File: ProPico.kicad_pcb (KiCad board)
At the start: 2 copper layers, 21 x 51 mm, 56 parts, among them J1 USB_C_Receptacle_USB2.0, J2 SWD, J3 LEFT, J4 RIGHT, SW1 BOOTSEL, SW2 RES, U1 FM24CL16B, U2 W25Q16JVUXIQ, U3 AMS1117-3.3, U4 LM4040DBZ-3, U5 RP2040, Y1 ECS-120-12-36-AGN-TR3

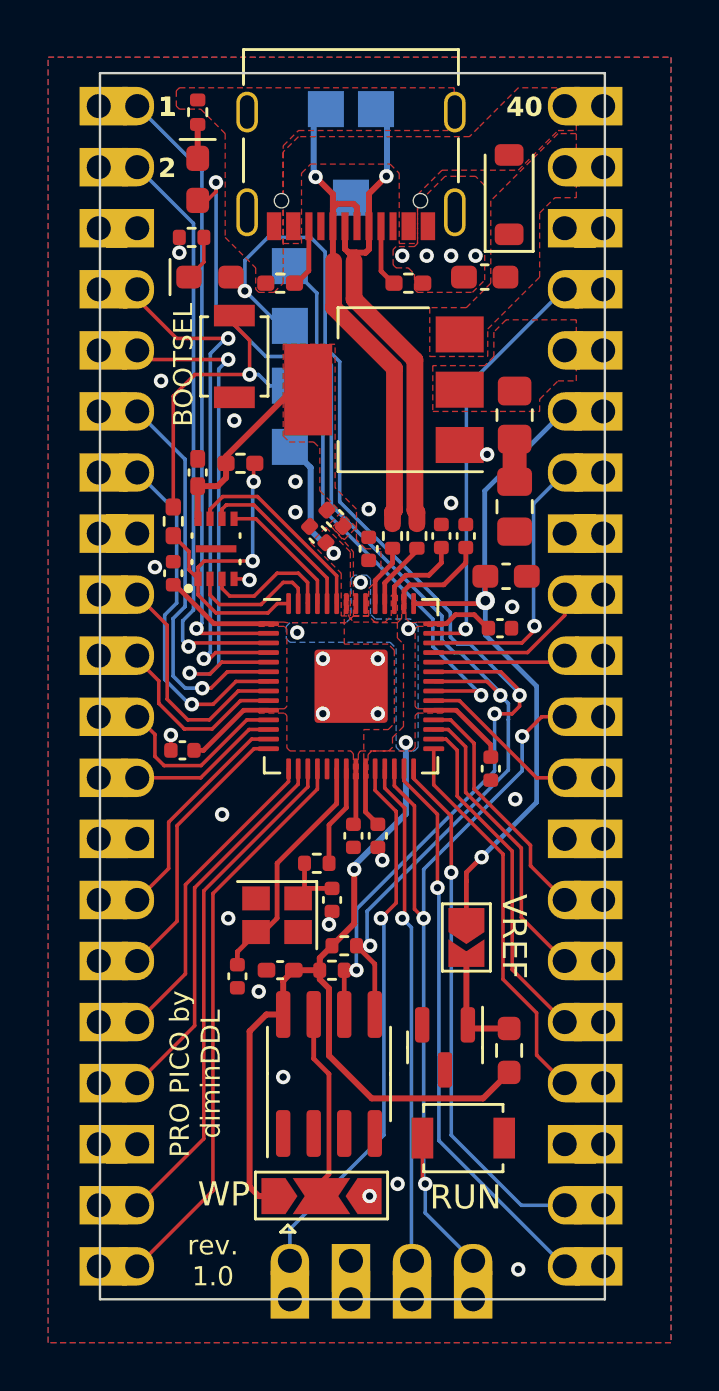
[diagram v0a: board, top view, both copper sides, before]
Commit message: Changed LDO for lower dropout
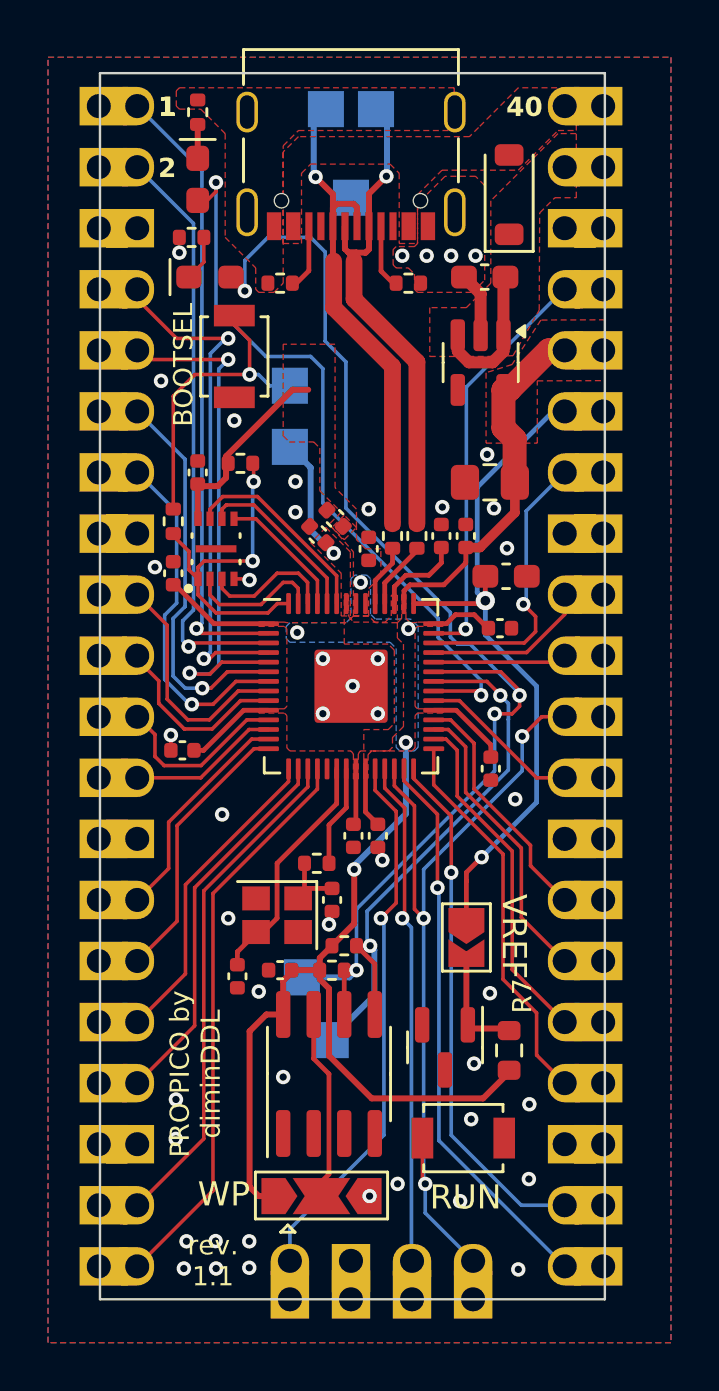
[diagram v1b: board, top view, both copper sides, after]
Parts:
- removed R6: 470mOhm, Resistor_SMD:R_0805_2012Metric_Pad1.20x1.40mm_HandSolder
- C1, C5: footprint Capacitor_SMD:C_0402_1005Metric_Pad0.74x0.62mm_HandSolder -> Capacitor_SMD:C_0402_1005Metric
- C4: value 2.2u -> 22u
- C6: value 10u -> 22u
- R1, R2, R3, R4: footprint Resistor_SMD:R_0402_1005Metric_Pad0.72x0.64mm_HandSolder -> Resistor_SMD:R_0402_1005Metric
- R7: footprint Resistor_SMD:R_0603_1608Metric_Pad0.98x0.95mm_HandSolder -> Resistor_SMD:R_0603_1608Metric
- U3: value AMS1117-3.3 -> AP2112K-3.3; footprint Package_TO_SOT_SMD:SOT-223-3_TabPin2 -> Package_TO_SOT_SMD:SOT-23-5
- moved TP6 32.2 mm to (102.0, 79.5)
- moved TP3 27.1 mm to (100.8, 76.9)
- moved G*** 17.3 mm to (101.1, 63.8)
- moved U3 4.18 mm to (108.3, 51.4), turned to -90 degrees
- moved C6 1.44 mm to (108.7, 56.3), turned to 180 degrees
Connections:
- C6 pad 1: Net-(C6-Pad1) -> +3V3
- U3 pad 1: GND -> +5V
- U3 pad 2: +3V3 -> GND
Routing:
- net /EEPROM_SDA: track 41.4 -> 24.7 mm
- net +3V3: track 65.0 -> 76.5 mm
- net +5V: track 0.00 -> 6.07 mm
- net GND: track 1.30 -> 4.00 mm, vias 30 -> 46
- net Net-(C6-Pad1): track 1.77 -> 0.00 mm
- net /ADC_VREF: track 28.7 -> 29.2 mm
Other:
- board text added: "rev. 1.1"
- board text removed: "rev. 1.0"

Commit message: Added JLCPCB Design Rules; Fixed Silkscreen to allow for JLC manufacturing
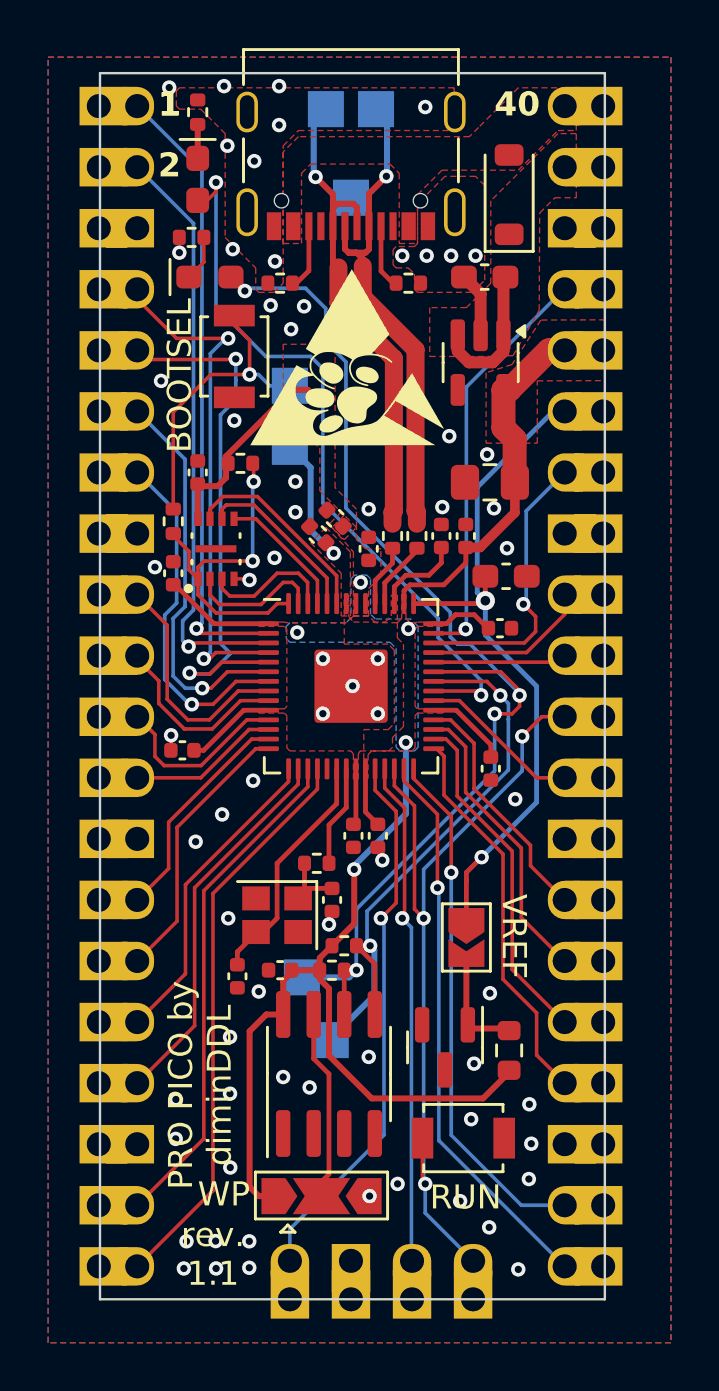
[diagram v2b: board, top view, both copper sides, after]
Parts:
- G***: moved to F.Cu
- moved G*** 12.6 mm to (102.9, 51.3), turned to 0 degrees
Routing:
- net /EEPROM_SCL: track 51.7 -> 47.8 mm
- net /GPIO3: track 21.7 -> 22.5 mm
- net GND: vias 46 -> 69
